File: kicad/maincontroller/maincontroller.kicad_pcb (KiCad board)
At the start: 2 copper layers, 56 x 71 mm, 22 parts, among them J1 XT60PW-M, J2 Screw_Terminal_01x05, U2 ESP32-S3-DEVKITC-1-N8R2, U3 LM2596S-3.3_NOPB, U4 LTC4311ISC6_TRPBF

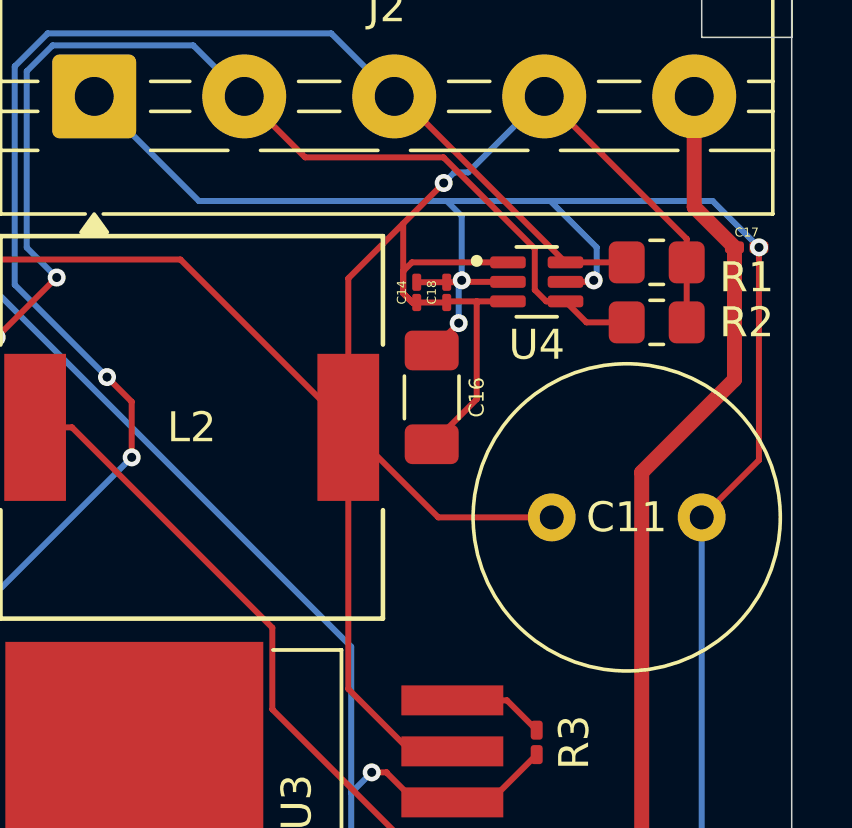
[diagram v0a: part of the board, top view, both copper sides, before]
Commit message: cleaned up kicad files and changed 1uf capacitors to 0805 SMD size
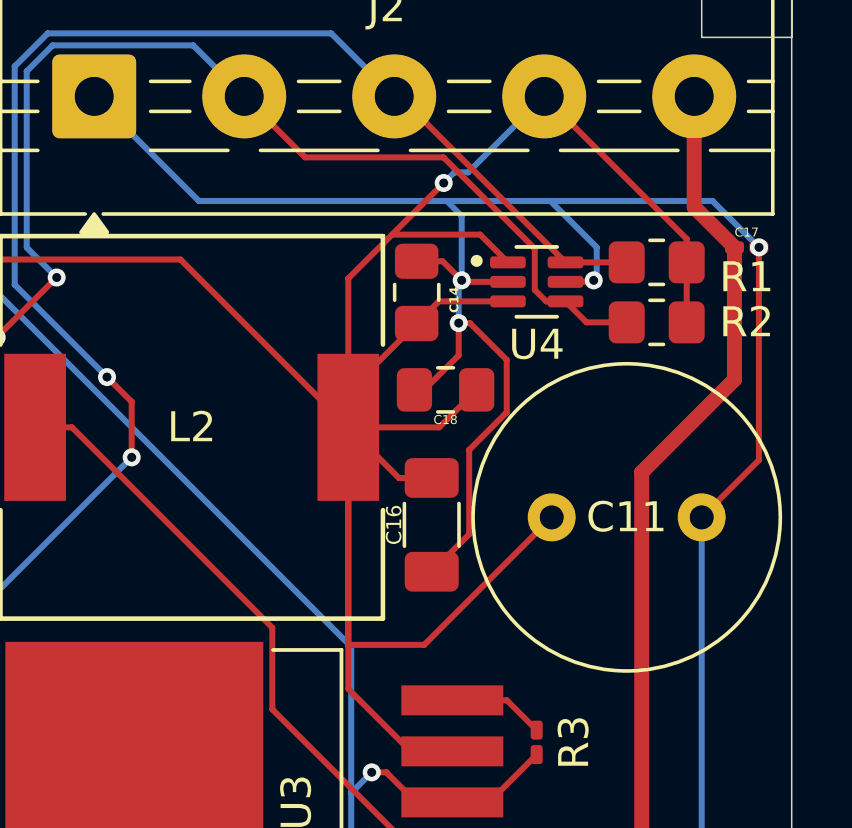
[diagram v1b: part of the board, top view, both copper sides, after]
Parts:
- C14, C18: footprint Capacitor_SMD:C_01005_0402Metric_Pad0.57x0.30mm_HandSolder -> Capacitor_SMD:C_0805_2012Metric_Pad1.18x1.45mm_HandSolder
- moved C16 4.25 mm to (157.0, 77.8), turned to -90 degrees
- moved C18 3.25 mm to (157.5, 73.2), turned to 180 degrees
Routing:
- net GND: track 255.1 -> 267.8 mm
- net +3.3V: track 106.2 -> 118.0 mm
